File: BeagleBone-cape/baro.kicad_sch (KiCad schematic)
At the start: 8 parts, among them IC3 BMP390

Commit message: Cape schematic: input protection, buzzer fix, CAN GND/jumper, LCSC field, lib refresh; ISSUES rewrite
Co-Authored-By: Claude Sonnet 5.5 <noreply@anthropic.com>
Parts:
- removed R8, R9: 4k7, Resistor_SMD:R_0603_1608Metric_Pad0.98x0.95mm_HandSolder, symbol Device:R_Small
- C1, C2: LCSC (none) -> C14663; LSCS Part Number C14663 -> (none)
- IC3: LCSC (none) -> C779278; LSCS Part Number C779278 -> (none)

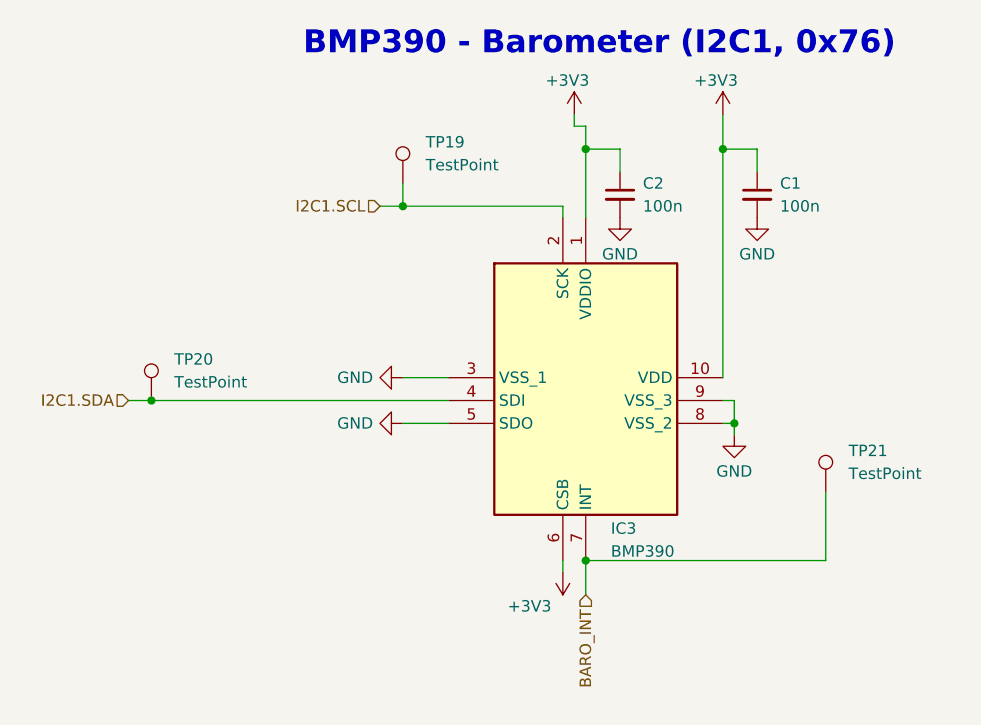
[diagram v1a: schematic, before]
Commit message: WIP: Q3 -> S-LP03N060TZHG (SOT-223), PCB synced with new schematic parts, not yet routed (DRC: shorts, 200 unconnected)
Co-Authored-By: Claude Sonnet 5.5 <noreply@anthropic.com>
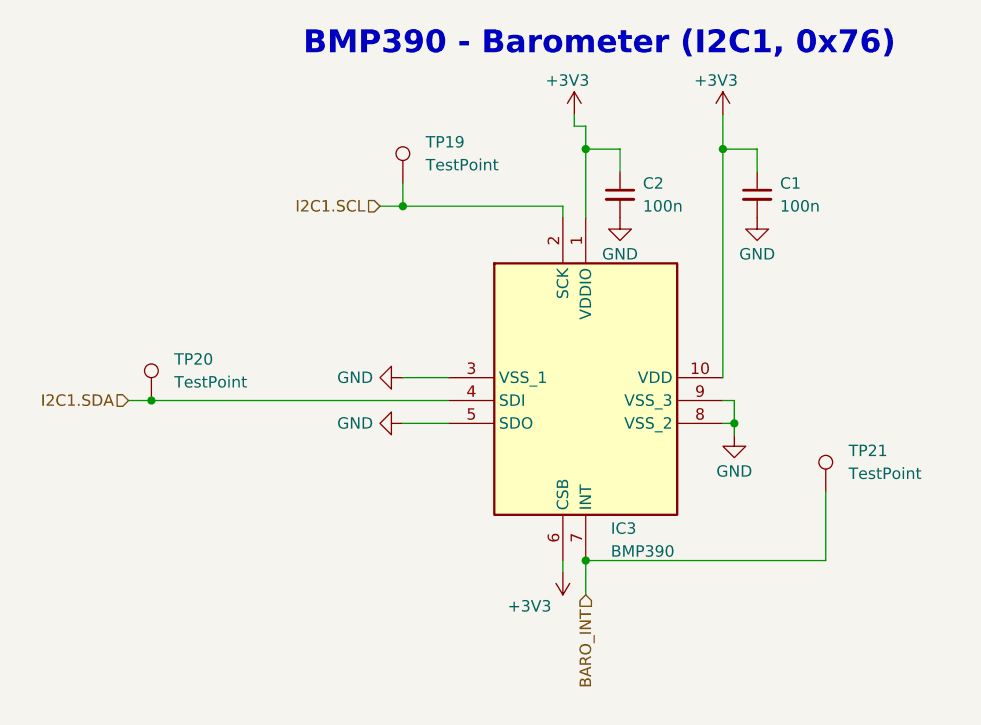
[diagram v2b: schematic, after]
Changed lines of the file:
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@@
 	(wire
 		(pts
-			(xy 104.14 104.14) (xy 118.11 104.14)
+			(xy 104.14 104.14) (xy 137.16 104.14)
 		)
 		(stroke
@@
 		)
 		(stroke
-			(width 0)
-			(type solid)
-		)
-	)
-	(wire
-		(pts
-			(xy 118.11 104.14) (xy 137.16 104.14)
-		)
-		(stroke
